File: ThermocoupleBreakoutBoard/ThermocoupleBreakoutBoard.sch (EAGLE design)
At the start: 30 parts

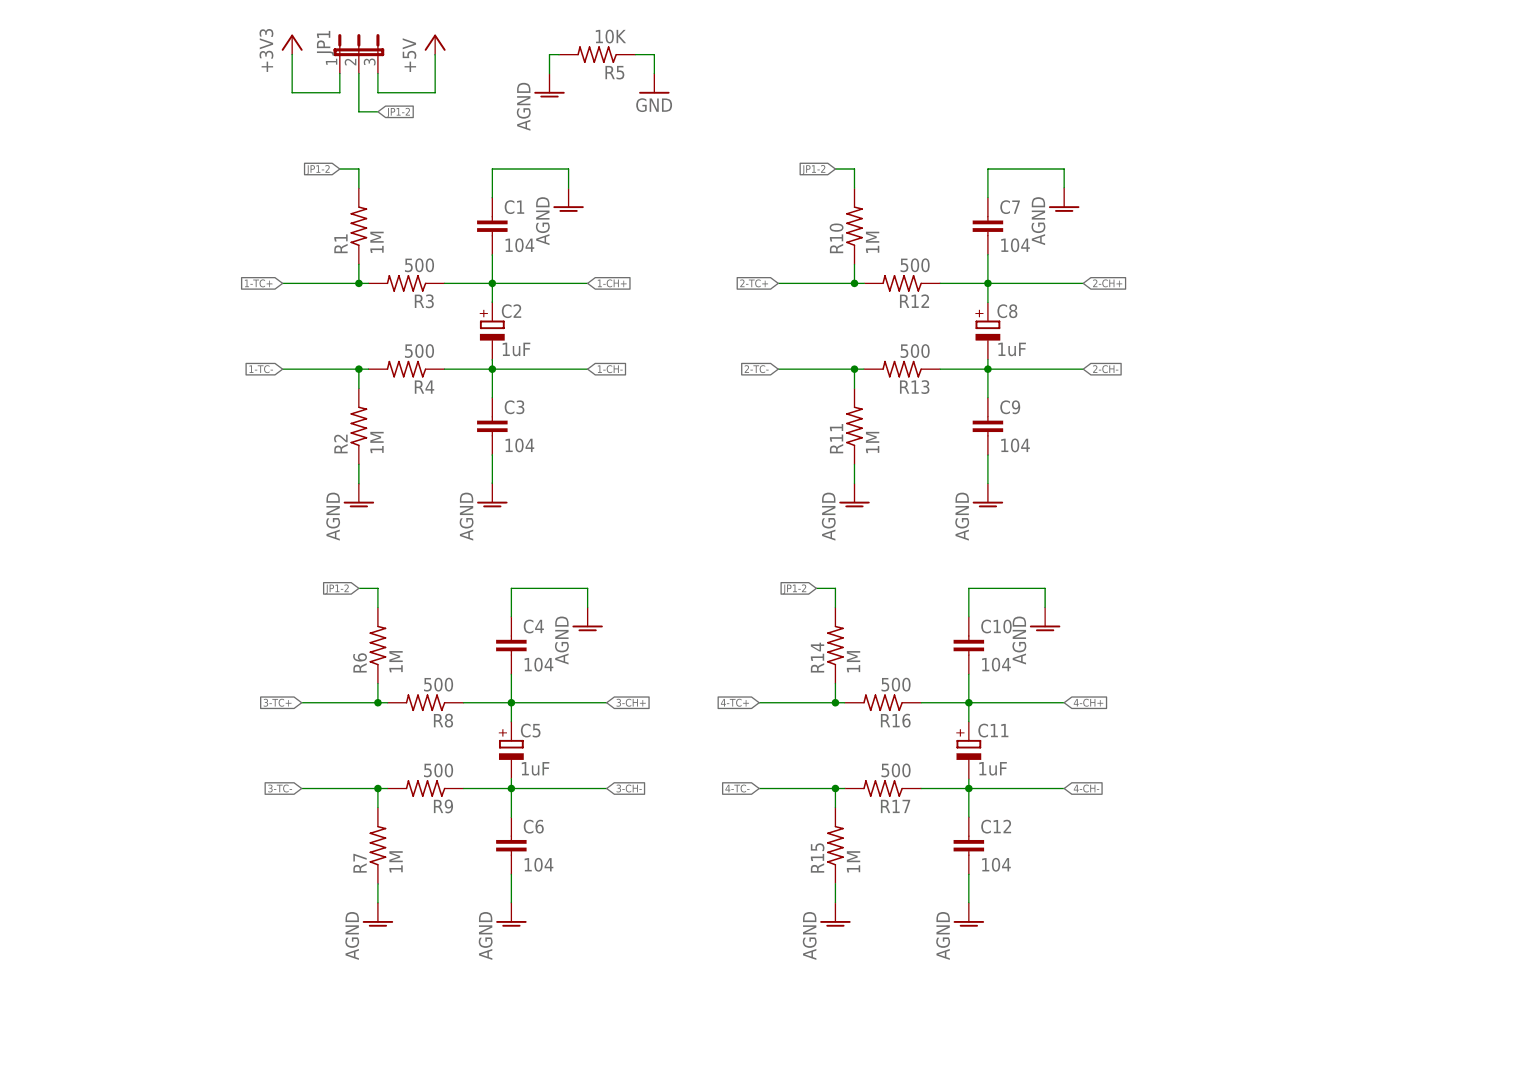
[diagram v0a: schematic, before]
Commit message: Added MCP3424 Device and made routing
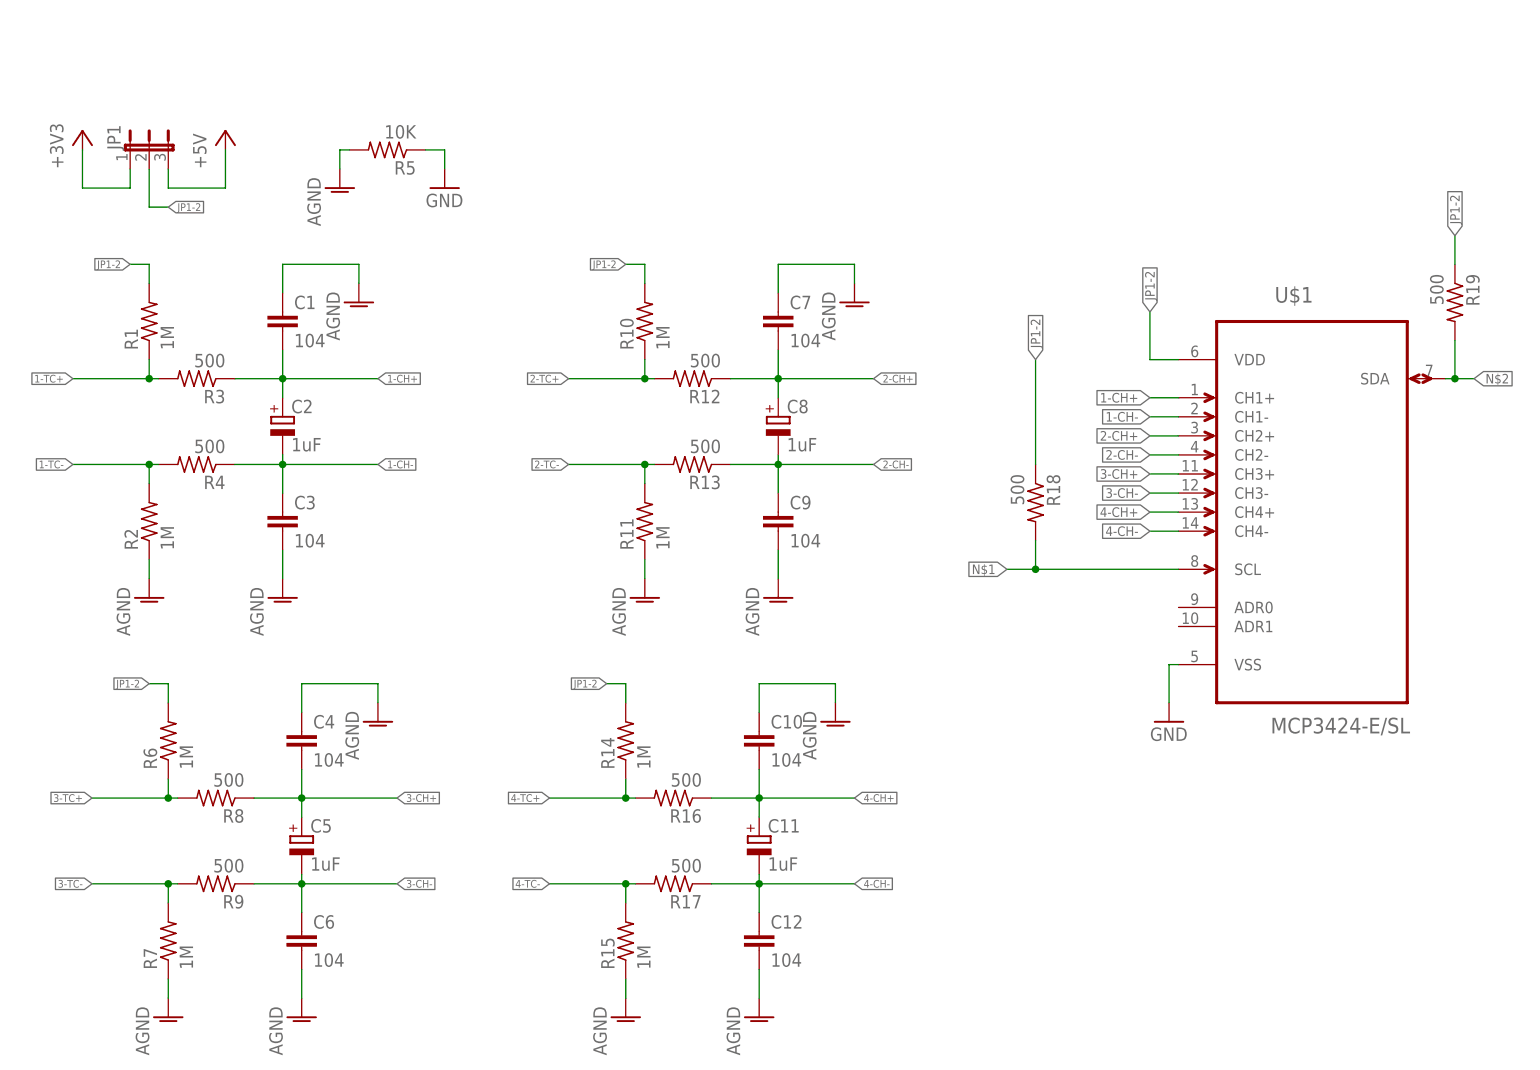
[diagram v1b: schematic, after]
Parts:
- added R18, R19: 500, rcl_vm:R-US_M1206
- added U$1: MCP3424-E/SL, i2c_devices:MCP3424-E/SL
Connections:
- new net N$1: R18.2, U$1.SCL
- new net N$2: R19.2, U$1.SDA
- net 1-CH+: now also U$1.CH1+
- net 1-CH-: now also U$1.CH1-
- net 2-CH+: now also U$1.CH2+
- net 2-CH-: now also U$1.CH2-
- net 3-CH+: now also U$1.CH3+
- net 3-CH-: now also U$1.CH3-
- net 4-CH+: now also U$1.CH4+
- net 4-CH-: now also U$1.CH4-
- net GND: now also U$1.VSS
- net JP1-2: now also R18.1, R19.1, U$1.VDD
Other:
- moved on the sheet: C1, C10, C11, C12, C2, C3, C4, C5, C6, C7, C8, C9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
